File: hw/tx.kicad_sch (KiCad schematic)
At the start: 53 parts, among them Q301 MMBF170, Q302 MMBF170, Q303 MMBF170, Q304 MMBF170, Q305 MMBF170, Q306 MMBF170, Q307 MMBF170, Q308 MMBF170, T301 BN-43-202_DualPri_CTSec, U301 SN74LVC1G74DCTR, U302 UCC27525DGN, U303 UCC27525DGN, U304 Si5351C-B-GM1, Y301 40MHz

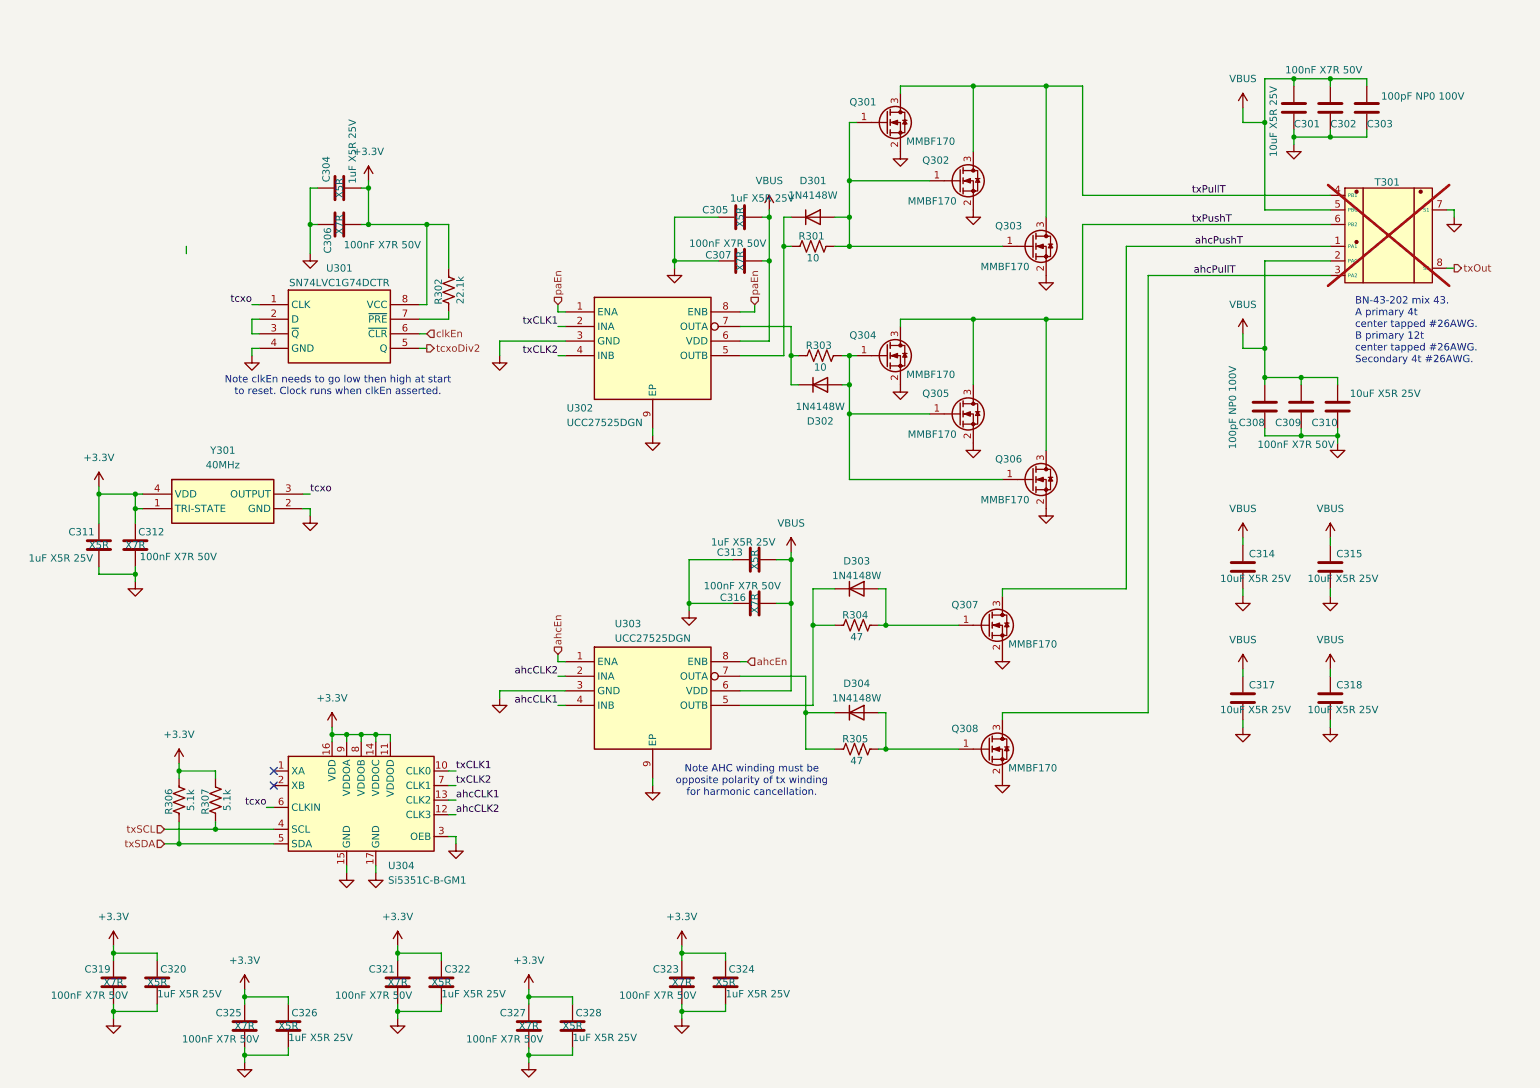
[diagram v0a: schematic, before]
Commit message: Now using RP2040 as a DDS. I can use SPI co-host to program its (SPI) flash. I can use I2C between ESP32 and RP2040 to send commands and receive status.
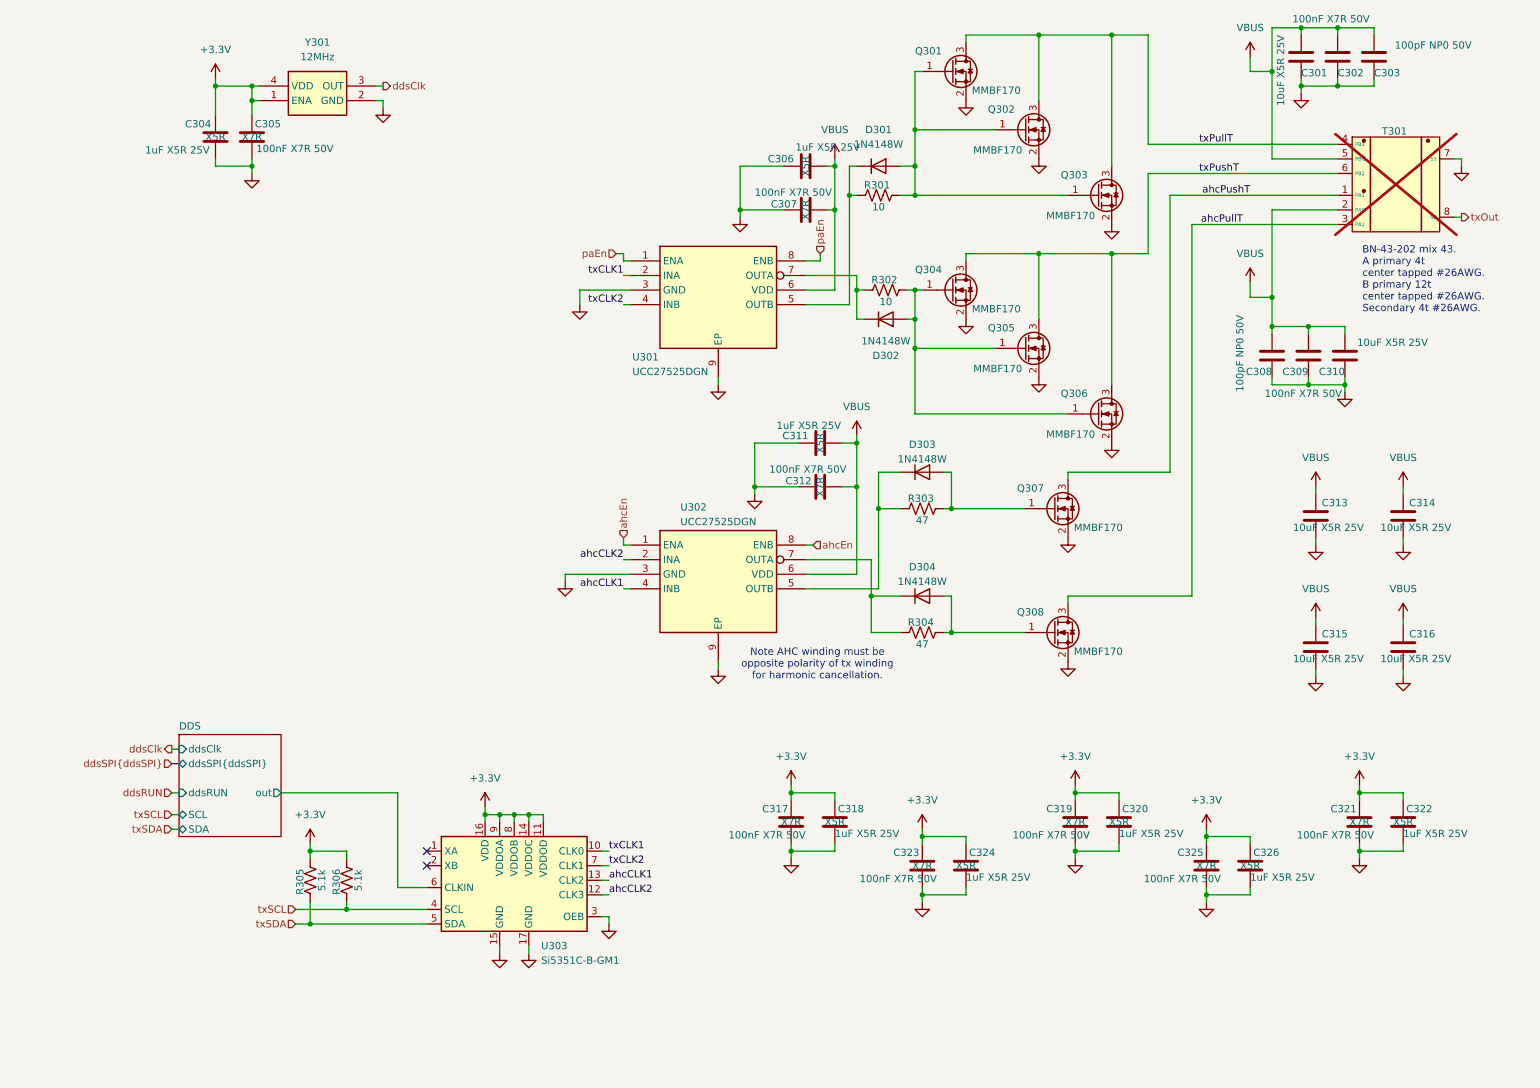
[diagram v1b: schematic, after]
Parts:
- removed C304: 1uF X5R 25V, Capacitor_SMD:C_0402_1005Metric, symbol Device:C
- removed C306: 100nF X7R 50V, Capacitor_SMD:C_0603_1608Metric, symbol Device:C
- removed R302: 22.1k, Resistor_SMD:R_0402_1005Metric, symbol Device:R_US
- removed U301: SN74LVC1G74DCTR, Package_SO:TSSOP-8_3x3mm_P0.65mm, symbol Library:SN74LVC1G74DCTR
- C302, C307, C309: footprint Capacitor_SMD:C_0603_1608Metric -> Capacitor_SMD:C_0402_1005Metric; LCSC C14663 -> (none); MPN KGM15BR71H104KT -> KAM05FR71H104KH; Mouser_PN 581-KGM15BR71H104KT -> (none)
- C303, C308: value 100pF NP0 100V -> 100pF NP0 50V; footprint Capacitor_SMD:C_0603_1608Metric -> Capacitor_SMD:C_0402_1005Metric; LCSC C76709 -> (none); MFG Kyocera AVX -> (none); MPN KGM15ACG2A101FT -> (none); Mouser_PN 581-KGM15ACG2A101FT -> (none)
- C305: renamed from C312; footprint Capacitor_SMD:C_0603_1608Metric -> Capacitor_SMD:C_0402_1005Metric; LCSC C14663 -> (none); MPN KGM15BR71H104KT -> KAM05FR71H104KH; Mouser_PN 581-KGM15BR71H104KT -> (none)
- C312: renamed from C316; footprint Capacitor_SMD:C_0603_1608Metric -> Capacitor_SMD:C_0402_1005Metric; LCSC C14663 -> (none); MPN KGM15BR71H104KT -> KAM05FR71H104KH; Mouser_PN 581-KGM15BR71H104KT -> (none)
- C317: renamed from C319; footprint Capacitor_SMD:C_0603_1608Metric -> Capacitor_SMD:C_0402_1005Metric; LCSC C14663 -> (none); MPN KGM15BR71H104KT -> KAM05FR71H104KH; Mouser_PN 581-KGM15BR71H104KT -> (none)
- C319: renamed from C321; footprint Capacitor_SMD:C_0603_1608Metric -> Capacitor_SMD:C_0402_1005Metric; LCSC C14663 -> (none); MPN KGM15BR71H104KT -> KAM05FR71H104KH; Mouser_PN 581-KGM15BR71H104KT -> (none)
- C321: renamed from C323; footprint Capacitor_SMD:C_0603_1608Metric -> Capacitor_SMD:C_0402_1005Metric; LCSC C14663 -> (none); MPN KGM15BR71H104KT -> KAM05FR71H104KH; Mouser_PN 581-KGM15BR71H104KT -> (none)
- C323: renamed from C325; footprint Capacitor_SMD:C_0603_1608Metric -> Capacitor_SMD:C_0402_1005Metric; LCSC C14663 -> (none); MPN KGM15BR71H104KT -> KAM05FR71H104KH; Mouser_PN 581-KGM15BR71H104KT -> (none)
- C325: renamed from C327; footprint Capacitor_SMD:C_0603_1608Metric -> Capacitor_SMD:C_0402_1005Metric; LCSC C14663 -> (none); MPN KGM15BR71H104KT -> KAM05FR71H104KH; Mouser_PN 581-KGM15BR71H104KT -> (none)
- Y301: value 40MHz -> 12MHz; footprint Library:ECSTXO201633400TR -> Library:Oscillator_SMD_AbraconATX-H12-4Pin_2.5x2.0mm; symbol Library:ECS-TXO-2016-33-400-TR -> Library:ASV-100.000MHZ-EC-T; Height 0.8 -> (none); LCSC C2451471 -> (none); MFG ECS -> (none); MPN ECS-TXO-2016-33-400-TR -> (none); Manufacturer ECS -> (none); Manufacturer_Name ECS -> (none); Manufacturer_Part_Number ECS-TXO-2016-33-400-TR -> (none); Mouser Part Number 520-TXO-2016-33-400T -> (none); Mouser Price/Stock https://www.mouser.co.uk/ProductDetail/ECS/ECS-TXO-2016-33-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 -> (none); Mouser_PN 520-TXO-2016-33-400T -> (none)
- renumbered C311 to C304, C305 to C306, C313 to C311, C314 to C313, C315 to C314, C317 to C315, C318 to C316, C320 to C318, C322 to C320, C324 to C322, C326 to C324, C328 to C326, R303 to R302, R304 to R303, R305 to R304, R306 to R305, R307 to R306, U302 to U301, U303 to U302, U304 to U303
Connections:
- net tcxo renamed DDS/out
- net DDS/out: no longer Y301.3 (OUTPUT)
- new net ddsClk: Y301.3 (OUT)
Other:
- added sheet DDS (dds.kicad_sch)
- note removed: "Note clkEn needs to go low then high at start to reset. Clock runs when clkEn asserted."
- moved on the sheet: C301, C302, C303, C304, C305, C306, C307, C308, C309, C310, C311, C312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

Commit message: Switched to SI5351 clocking MACHXO2 CPLD to drive gate driver for MOSFETs. It passes DRC but needs serious reviewing.
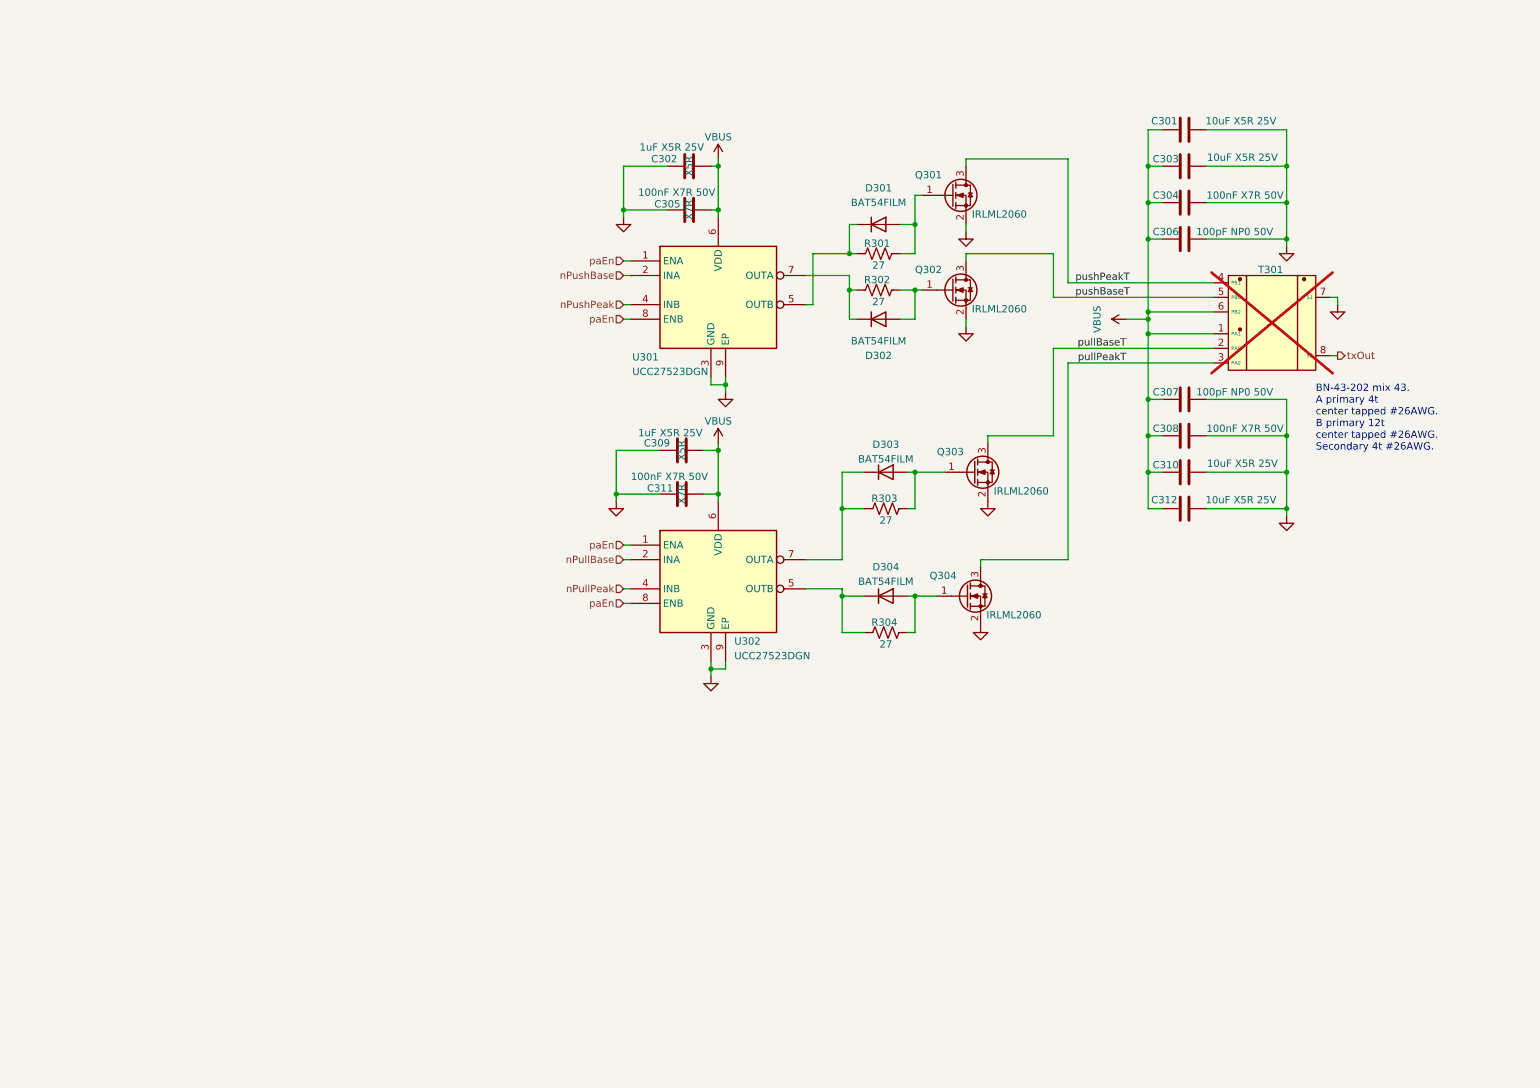
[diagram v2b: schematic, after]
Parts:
- removed C302, C305, C309, C317, C319, C321, C323, C325: 100nF X7R 50V, Capacitor_SMD:C_0402_1005Metric, symbol Device:C
- removed C313, C314, C315, C316: 10uF X5R 25V, Capacitor_SMD:C_0603_1608Metric, symbol Device:C
- removed C318, C320, C322, C324, C326: 1uF X5R 25V, Capacitor_SMD:C_0402_1005Metric, symbol Device:C
- removed Q305, Q306, Q307, Q308: MMBF170, Package_TO_SOT_SMD:SOT-23, symbol Transistor_FET:BS170F
- removed R305, R306: 5.1k, Resistor_SMD:R_0402_1005Metric, symbol Device:R_US
- removed U303: Si5351C-B-GM1, Library:QFN50P300X300X90-17N-D, symbol Library:Si5351C-B-GM1
- removed Y301: 12MHz, Library:Oscillator_SMD_AbraconATX-H12-4Pin_2.5x2.0mm, symbol Library:ASV-100.000MHZ-EC-T
- added C306, C307: 100pF NP0 50V, Capacitor_SMD:C_0402_1005Metric, symbol Device:C
- added C312: 10uF X5R 25V, Capacitor_SMD:C_0603_1608Metric, symbol Device:C
- C303: value 100pF NP0 50V -> 10uF X5R 25V; footprint Capacitor_SMD:C_0402_1005Metric -> Capacitor_SMD:C_0603_1608Metric; LCSC (none) -> C479655; MFG (none) -> Kyocera AVX; MPN (none) -> CM105X5R106M25AT; Mouser_PN (none) -> 346-CM105X5R106M25AT; cap-type NP0 -> X5R; working-voltage 50V -> 25V
- C304: value 1uF X5R 25V -> 100nF X7R 50V; LCSC C7393852 -> (none); MPN 04023D105MAT2A -> KAM05FR71H104KH; Manufacturer Murata -> (none); Mouser_PN 581-04023D105MAT2A -> (none); cap-type X5R -> X7R; working-voltage 25V -> 50V
- C308: value 100pF NP0 50V -> 100nF X7R 50V; MFG (none) -> Kyocera AVX; MPN (none) -> KAM05FR71H104KH; cap-type NP0 -> X7R
- D301, D302, D303, D304: value 1N4148W -> BAT54FILM; LCSC C51953478 -> (none); MFG Diodes Inc -> ST; MPN 1N4148W-7-F -> BAT54ZFILM; Mouser_PN 621-1N4148W-F -> 511-BAT54FILM
- Q301, Q302, Q303, Q304: value MMBF170 -> IRLML2060; LCSC C151058 -> (none); MFG Diodes inc -> Infineon; MPN MMBF170Q-13-F -> IRLML2060TRPBF; Mouser_PN 621-MMBF170Q-13-F -> 942-IRLML2060TRPBF
- R301, R302: value 10 -> 27; footprint Resistor_SMD:R_0603_1608Metric -> Resistor_SMD:R_0402_1005Metric; LCSC C2784788 -> (none); MFG Vishay -> (none); MPN MCT06030C1009FP500 -> (none); Mouser_PN 594-MCT06030C1009FP5 -> (none)
- R303, R304: value 47 -> 27; LCSC C2479306 -> (none); MFG Yageo -> (none); MPN AC0402FR-0747RL -> (none); Mouser_PN 603-AC0402FR-0747RL -> (none)
- U301, U302: value UCC27525DGN -> UCC27523DGN; symbol Library:UCC27525DGN -> Library:UCC27523DGN
- renumbered C306 to C302, C307 to C305, C311 to C309, C312 to C311
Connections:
- net +3.3V is gone; now on net VBUS: C304.1
- net ahcEn is gone; now on net paEn: U302.1 (ENA), U302.8 (ENB)
- net ahcPushT is gone; now on net VBUS: T301.1 (PA1)
- net GND: now also C301.2, C303.2, C308.2, C310.2, C306.2, C307.2, C312.2; no longer C301.1, C303.1, C308.1, C310.1
- net VBUS: now also C301.1, C303.1, C308.1, C310.1, T301.6 (PB2), C306.1, C307.1, C312.1; no longer C301.2, C303.2, C308.2, C310.2, T301.2 (PAC), T301.5 (PBC)
- net at D302.2 (A), R302.2: now also Q302.1 (G); no longer Q304.1 (G)
- net at D303.1 (K), R303.1: now also U302.7 (OUTA); no longer U302.5 (OUTB)
- net at D303.2 (A), R303.2: now also Q303.1 (G)
- net at D301.2 (A), Q301.1 (G), R301.2: no longer Q302.1 (G), Q303.1 (G)
- net at D304.2 (A), R304.2: now also Q304.1 (G)
- net at D304.1 (K), R304.1: now also U302.5 (OUTB); no longer U302.7 (OUTA)
- net ahcCLK1 renamed nPullPeak
- net ahcCLK2 renamed nPullBase
- net ahcPullT renamed pullPeakT
- net pullPeakT: now also Q304.3 (D)
- net txCLK1 renamed nPushBase
- net txCLK2 renamed nPushPeak
- net txPullT renamed pushPeakT
- net pushPeakT: no longer Q302.3 (D), Q303.3 (D)
- removed net txPushT: Q304.3 (D), T301.6 (PB2)
- new net pullBaseT: Q303.3 (D), T301.2 (PAC)
- new net pushBaseT: Q302.3 (D), T301.5 (PBC)
- no-connect marks 2 -> 0
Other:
- removed sheet DDS
- note removed: "Note AHC winding must be opposite polarity of tx winding for harmonic cancellation."
- moved on the sheet: C302, C305, C309, C311, D301, D302, D303, D304, Q301, R301, R302, R303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
